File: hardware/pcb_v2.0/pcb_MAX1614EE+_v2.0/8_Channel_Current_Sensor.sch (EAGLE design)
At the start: 46 parts, among them Q1 BSS138, Q2 BSS138, SW1 DIP-SLIDE-SWITCH-EG1218

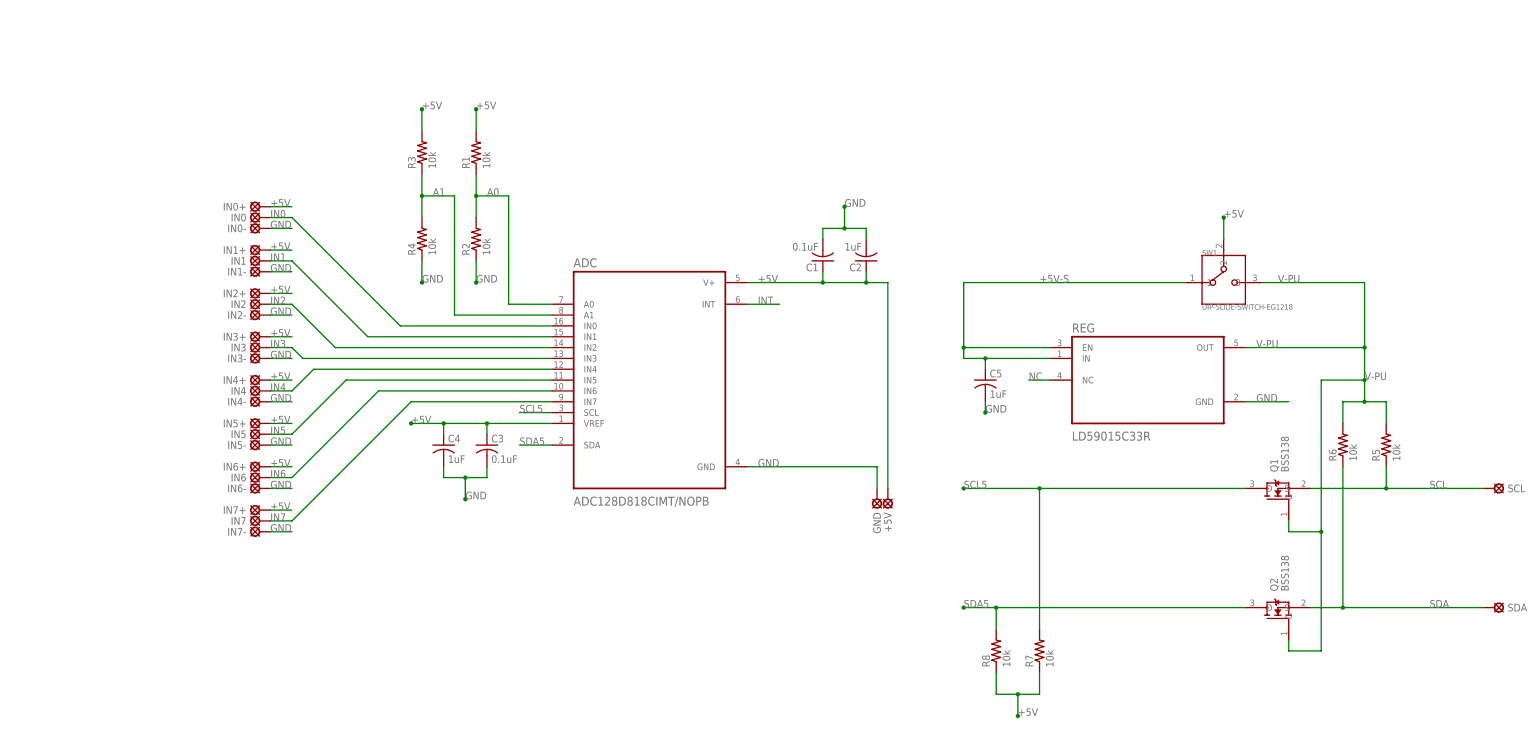
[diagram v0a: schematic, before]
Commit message: New PCB designs, reorganized files, removed clutter
Added pcb v1.2 the final draft of the ADC12818 board.
Added pcb v2.0 the new board boased on the MAX1614EE+ ADC
Added datasheet for MAX ADC
Renamed folders to have consistent naming scheme
Removed unncessary tempoary files
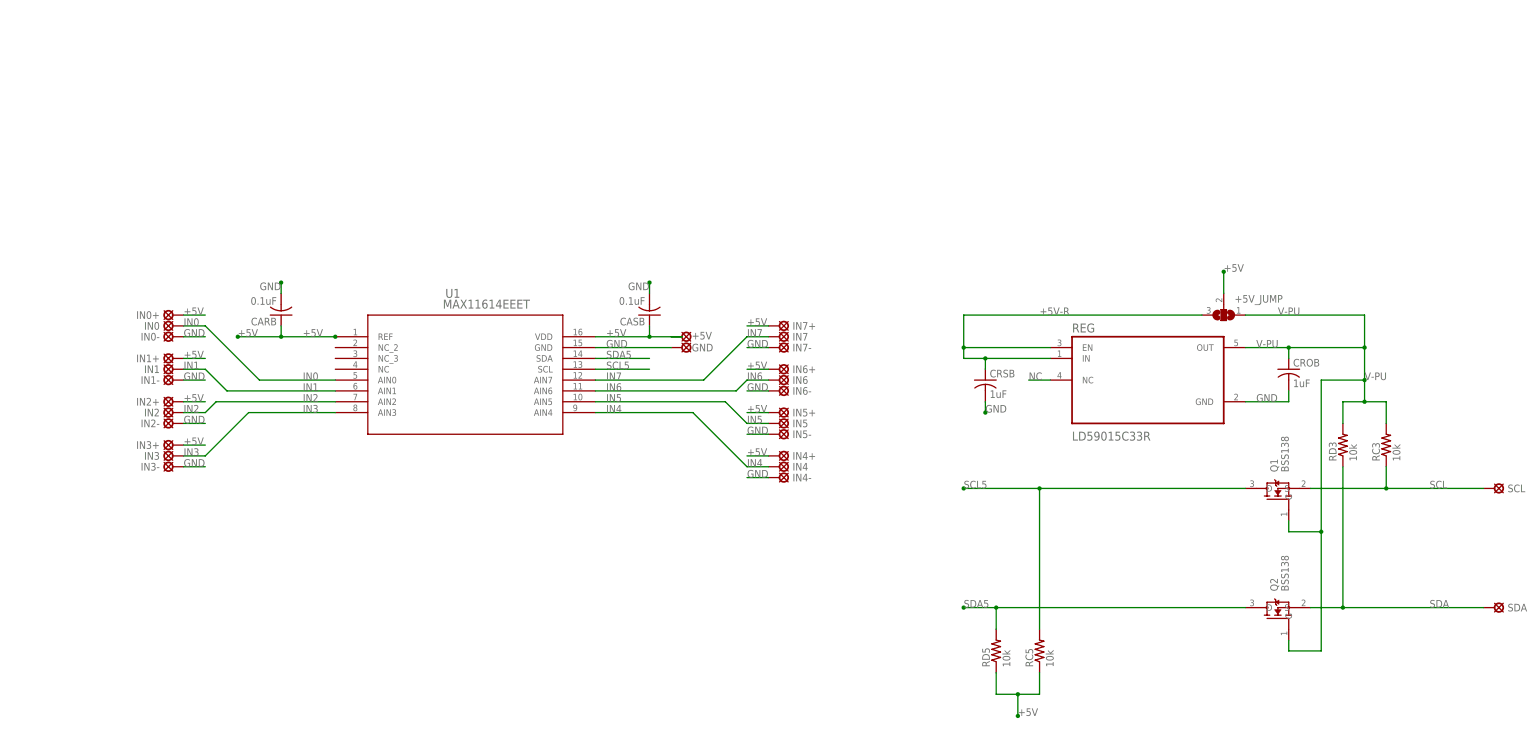
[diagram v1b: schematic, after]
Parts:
- removed ADC: ADC128D818CIMT/NOPB, ADC128D818CIMT_NOPB:ADC128D818CIMT/NOPB
- removed C1, C3: 0.1uF, resistor:C-USC0603
- removed C2, C4: 1uF, resistor:C-USC0603
- removed R1, R2, R3, R4: 10k, resistor:R-US_R0603
- removed SW1: DIP-SLIDE-SWITCH-EG1218, EG1218-DIP-SLIDE-SWITCH:DIP-SLIDE-SWITCH-EG1218
- added +5V_JUMP: (no value), jumper:SJ2W
- added CARB, CASB: 0.1uF, resistor:C-USC0603
- added CROB: 1uF, resistor:C-USC0603
- added U1: MAX11614EEET, MAX11614EEET:MAX11614EEET
- renumbered C5 to CRSB, R5 to RC3, R6 to RD3, R7 to RC5, R8 to RD5
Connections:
- removed net +5V-S: CRSB.1, REG.EN, REG.IN, SW1.1
- removed net A0: ADC.A0, R1.1, R2.2
- removed net A1: ADC.A1, R3.1, R4.2
- removed net INT: ADC.INT
- new net +5V-R: +5V_JUMP.3, CRSB.1, REG.EN, REG.IN
- net +5V: now also +5V_JUMP.2, CARB.1, CASB.1, U1.REF, U1.VDD; no longer ADC.V+, ADC.VREF, C1.1, C2.1, C3.1, C4.1, R1.2, R3.2, SW1.2
- net GND: now also CARB.2, CASB.2, CROB.2, U1.GND; no longer ADC.GND, C1.2, C2.2, C3.2, C4.2, R2.1, R4.1
- net IN0: now also U1.AIN0; no longer ADC.IN0
- net IN1: now also U1.AIN1; no longer ADC.IN1
- net IN2: now also U1.AIN2; no longer ADC.IN2
- net IN3: now also U1.AIN3; no longer ADC.IN3
- net IN4: now also U1.AIN4; no longer ADC.IN4
- net IN5: now also U1.AIN5; no longer ADC.IN5
- net IN6: now also U1.AIN6; no longer ADC.IN6
- net IN7: now also U1.AIN7; no longer ADC.IN7
- net SCL5: now also U1.SCL; no longer ADC.SCL
- net SDA5: now also U1.SDA; no longer ADC.SDA
- net V-PU: now also +5V_JUMP.1, CROB.1; no longer SW1.3
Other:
- moved on the sheet: +5V, GND, IN0, IN0+, IN0-, IN1, IN1+, IN1-, IN2, IN2+, IN2-, IN3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

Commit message: Finished v2 of ADC board
Completed changes to ADC board and parts list.
Changes:
-Added header for voltage directly from the battery
-Added voltage divider to measure battery voltage
-Added buck converter to make clean 5V from battery voltage
-Switched to more accurate MAX1614 ADC
-Rearranged components and added solder jumpers as appropriate
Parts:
- removed +5V: LSP10, solpad:LSP10
- removed +5V_JUMP: (no value), jumper:SJ2W
- removed REG: LD59015C33R, LD59015C33R:LD59015C33R
- added 3V3REG: LD59015C33R, LD59015C33R:LD59015C33R
- added 5VBUCK: ACT4088US-T, ACT4088US-T:ACT4088US-T
- added C1: 10uF, resistor:C-USC0603K
- added C2, C3: 22uF, resistor:C-USC0603K
- added CVD: 0.1uF, resistor:C-USC0603K
- added D1: NSR20F30NXT5G, NSR20F30NXT5G:NSR20F30NXT5G
- added G, V+, VCC: LSP10, solpad:LSP10
- added JUMP_+5V, JUMP_CH0, JUMP_VI2C: (no value), jumper:SJ2W
- added L1: 4.7uF, rc-master-smd:L_PM1008
- added RDV2, RFB2: 9.65k, resistor:R-US_R0603
- added RFB1, RVD1: 49.9k, resistor:R-US_R0603
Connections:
- new net BST: 5VBUCK.BST, C3.2
- new net CH0: JUMP_CH0.2, U1.AIN0
- new net FB: 5VBUCK.FB, RFB1.1, RFB2.2
- new net IN: 5VBUCK.IN, C1.1, RVD1.2, V+.MP
- new net SW: 5VBUCK.SW, C3.1, D1.C, L1.2
- new net VCC: JUMP_+5V.3, VCC.MP
- new net VD: CVD.1, JUMP_CH0.3, RDV2.2, RVD1.1
- new net VR+: C2.1, JUMP_+5V.1, L1.1, RFB1.2
- net +5V: now also JUMP_+5V.2, JUMP_VI2C.2; no longer +5V.MP, +5V_JUMP.2
- net +5V-R: now also 3V3REG.EN, 3V3REG.IN, JUMP_VI2C.3; no longer +5V_JUMP.3, REG.EN, REG.IN
- net GND: now also 3V3REG.GND, 5VBUCK.G, C1.2, C2.2, CVD.2, D1.A, G.MP, RDV2.1, RFB2.1; no longer REG.GND
- net IN0: now also JUMP_CH0.1; no longer U1.AIN0
- net NC: now also 3V3REG.NC; no longer REG.NC
- net V-PU: now also 3V3REG.OUT, JUMP_VI2C.1; no longer +5V_JUMP.1, REG.OUT
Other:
- moved on the sheet: CROB, CRSB, GND, IN0, IN0+, IN0-, Q1, Q2, RC3, RC5, RD3, RD5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
